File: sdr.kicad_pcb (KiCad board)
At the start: 4 copper layers, 65 x 56 mm, 162 parts, among them J1 SMA_H, J2 SMA_H, T1 B0322J5050, T2 B0322J5050, U1 FT601, U10 MIC94310, U11 PAM2305, U2 ESD7016, U3 LMS6002DR2, U4 ECP5, U5 Si5351, U6 PAM2305, U7 NCP186, U8 MIC94310, U9 MIC94310, X1 GSB443133HR, X2 CONN_01X08, X3 RaspberryPiConnector, Y1 FL3000027, Y2 ABM11-141-26.000MHZ

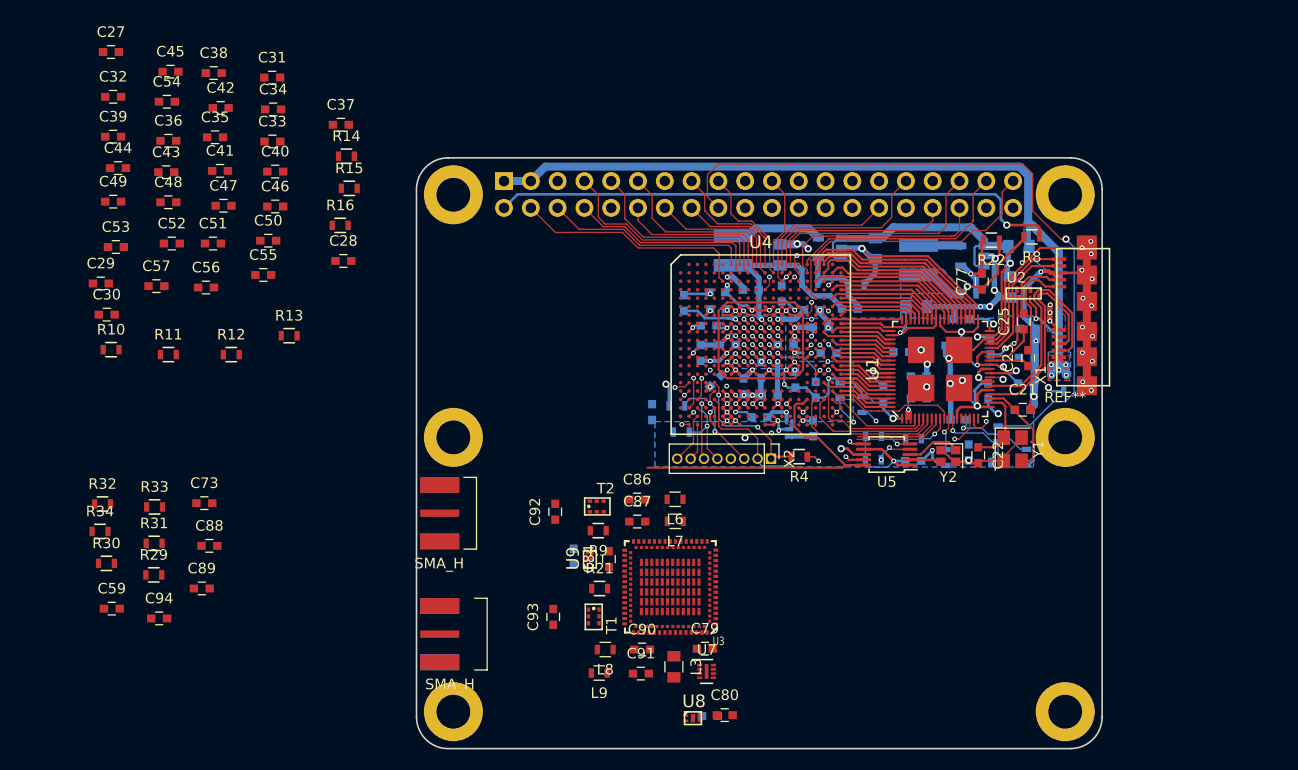
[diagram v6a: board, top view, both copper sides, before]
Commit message: Fix bug with not traced FT_TXE FT_RXF
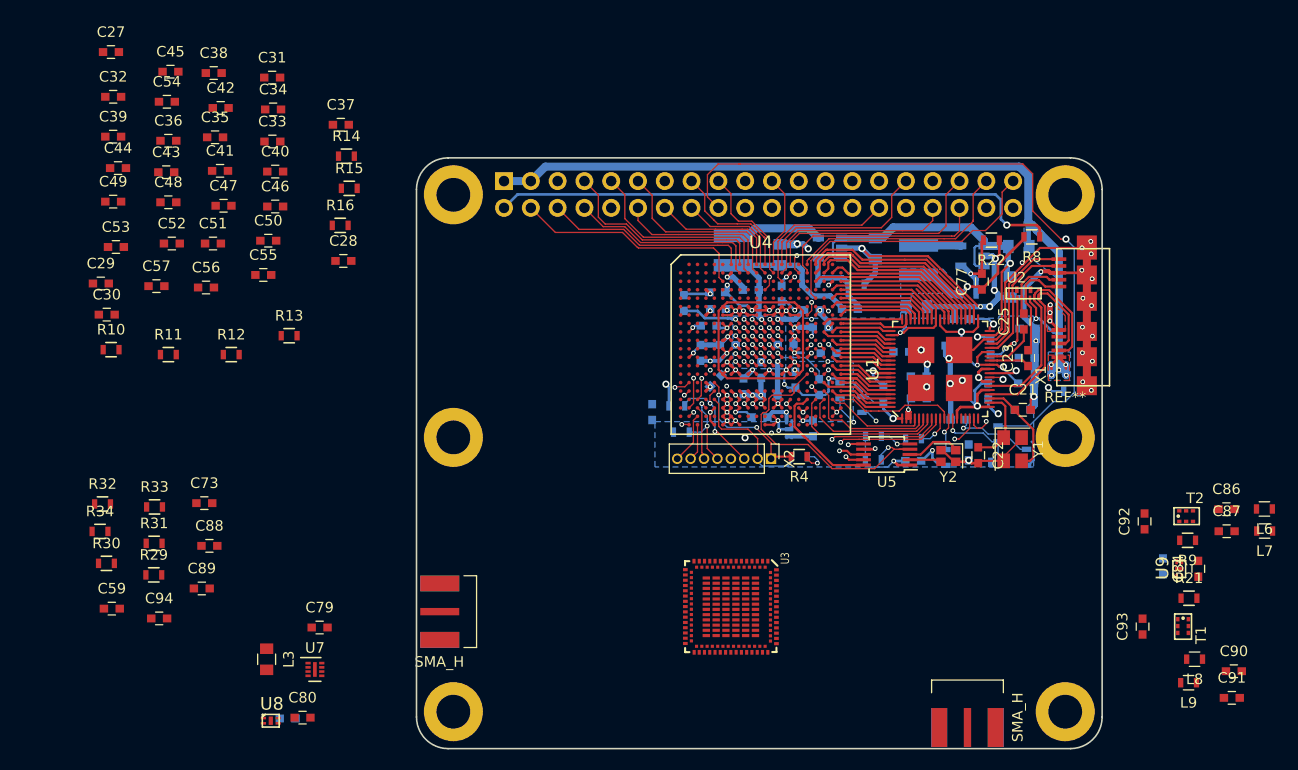
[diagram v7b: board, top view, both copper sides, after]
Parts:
- moved C90 56.1 mm to (177.5, 148.7)
- moved C91 56.1 mm to (177.3, 151.2)
- moved C81 55.9 mm to (170.8, 138.7)
- moved L6 55.9 mm to (180.4, 133.3)
- moved L8 55.9 mm to (173.8, 147.5)
- moved R21 55.9 mm to (173.2, 141.7)
- moved R9 55.9 mm to (173.1, 136.3)
- moved T1 55.9 mm to (172.2, 145.0)
- moved C84 55.9 mm to (174.1, 139.0)
- moved C86 55.9 mm to (176.8, 133.3)
- moved C87 55.9 mm to (176.8, 135.4)
- moved C92 55.9 mm to (169.0, 134.5)
- moved C93 55.9 mm to (168.8, 144.4)
- moved L7 55.9 mm to (180.4, 135.4)
- moved T2 55.9 mm to (173.6, 134.5)
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- renumbered R20 to R19, R19 to R20
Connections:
- U4 pad P16: Net-(U4-PadP16) -> /FT601/I2C_SCL
- U4 pad P17: /FT601/I2C_SDA -> /FT601/~FT_TXE
- U4 pad T17: Net-(U4-PadT17) -> /FT601/~FT_RXF
- U4 pad Y2: /FT601/I2C_SCL -> /FT601/I2C_SDA
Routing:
- net CLK0: track 31.2 -> 13.8 mm
- net /FT601/I2C_SDA: track 15.3 -> 26.7 mm
- net /FT601/~FT_TXE: track 8.07 -> 18.6 mm, vias 0 -> 2
- net /FT601/~FT_RXF: track 8.66 -> 18.2 mm, vias 0 -> 2
- net LMS_D3V3: track 134.9 -> 132.7 mm, vias 23 -> 24
- net /FT601/I2C_SCL: track 25.8 -> 27.8 mm, vias 3 -> 1
- net FT_GPIO1: track 79.2 -> 78.6 mm
- net CLK2: track 13.2 -> 12.7 mm
- net +1V1: track 48.1 -> 48.6 mm

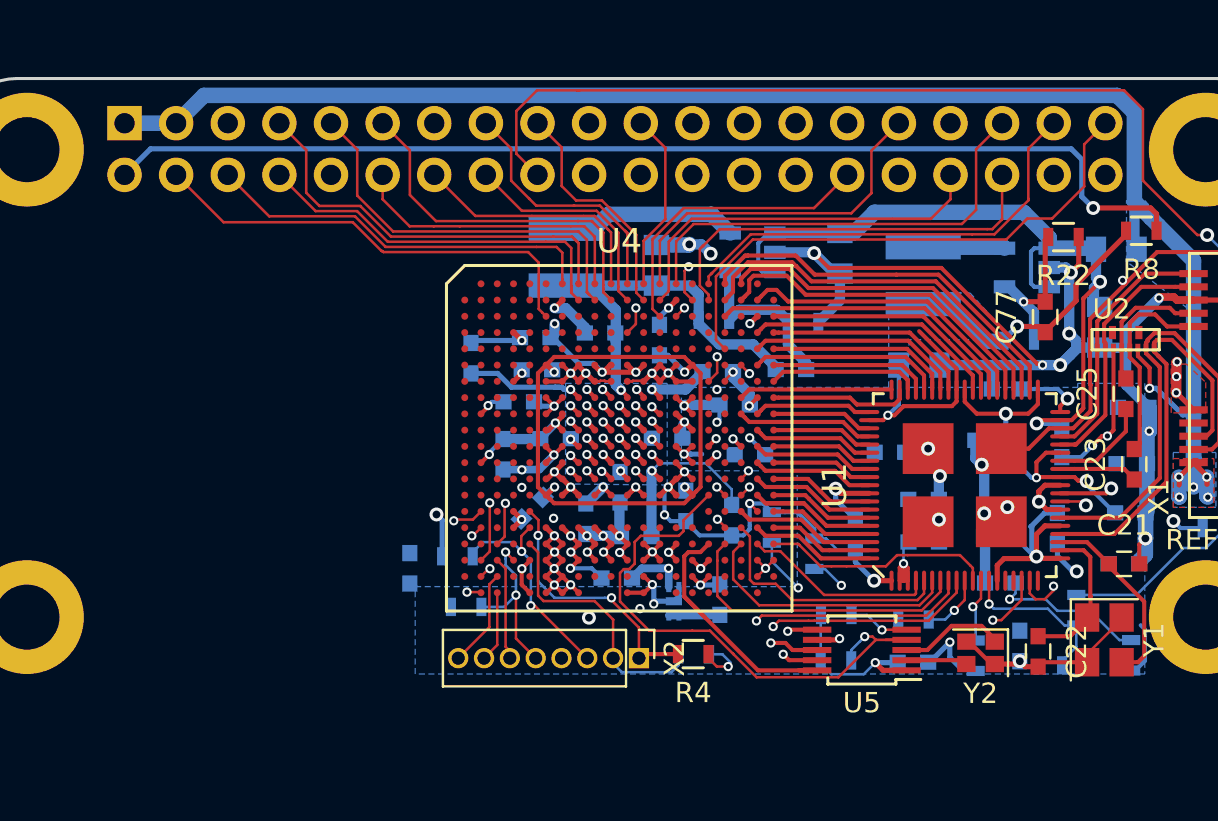
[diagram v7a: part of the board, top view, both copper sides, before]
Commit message: Finish tracing all except SDRAM and AFE
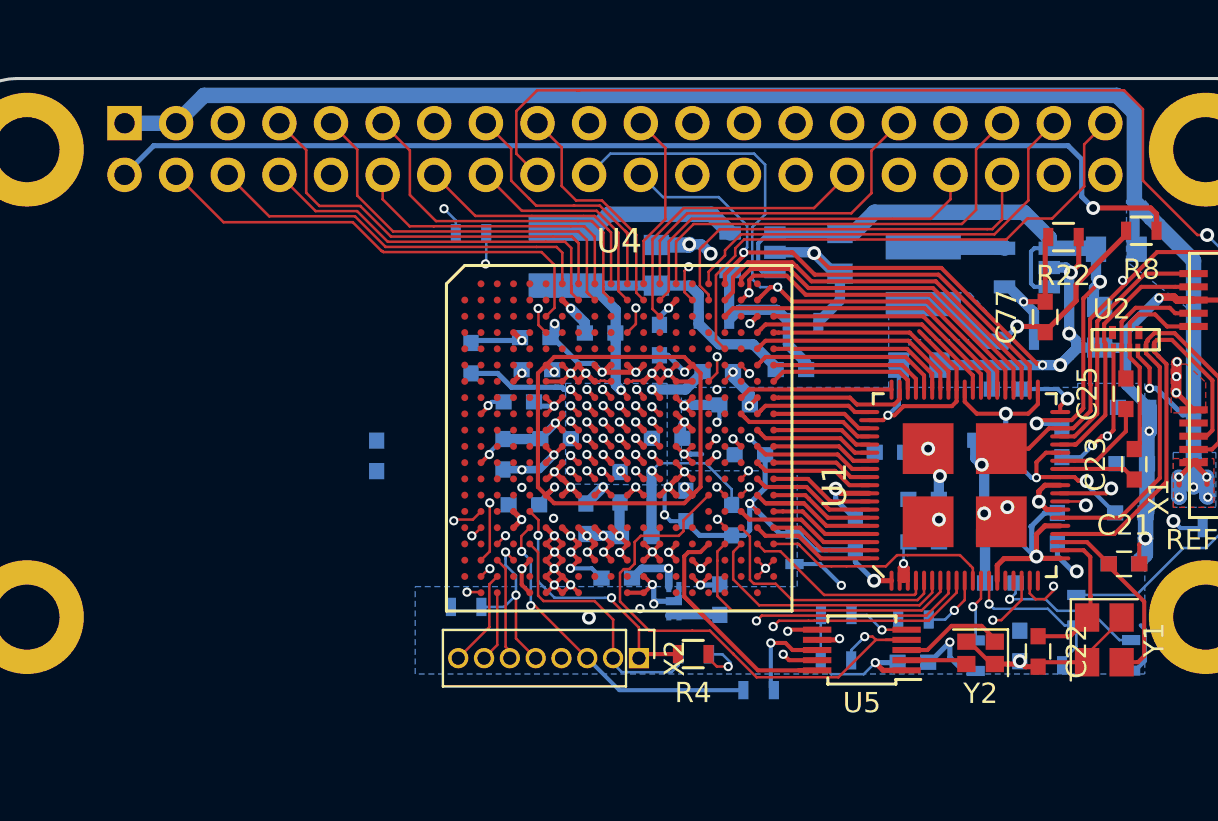
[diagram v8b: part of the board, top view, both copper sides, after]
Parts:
- moved R18 20.7 mm to (125.3, 107.6), turned to 180 degrees
- moved R6 16.2 mm to (139.5, 130.1), turned to 180 degrees
- moved C78 5.77 mm to (120.7, 118.6)
- moved R17 1.01 mm to (141.3, 123.1)
- moved C60 0.44 mm to (127.9, 121.0), turned to 180 degrees
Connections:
- U1 pad 40: FT_D0 -> CFG_MISO
- U1 pad 43: FT_D3 -> CFG_MCLK
- U1 pad 44: FT_D4 -> CFG_MOSI
- U4 pad A17: FT_D0 -> CFG_MISO
- U4 pad B18: FT_D3 -> CFG_MCLK
- U4 pad B19: FT_D4 -> CFG_MOSI
- U4 pad D6: Net-(U4-PadD6) -> CFG_MCLK
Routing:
- net CFG_MOSI: track 22.4 -> 53.7 mm, vias 1 -> 2
- net CFG_MCLK: track 25.1 -> 52.6 mm, vias 1 -> 3
- net CFG_MISO: track 23.5 -> 50.7 mm, vias 1 -> 2
- net FT_D0: track 19.2 -> 0.00 mm
- net FT_D3: track 16.7 -> 0.00 mm
- net FT_D4: track 14.6 -> 0.00 mm
- net FT_GPIO1: track 78.6 -> 72.4 mm
- net /Power/TCK: track 11.1 -> 16.4 mm
- net GNDD: track 253.8 -> 257.9 mm
- net LMS_D3V3: track 132.7 -> 134.3 mm
- net FT_GPIO0: track 13.0 -> 14.1 mm
- net RPI_A3: track 22.4 -> 23.1 mm
- net Net-(U4-PadC14): track 0.58 -> 0.00 mm, vias 1 -> 0
